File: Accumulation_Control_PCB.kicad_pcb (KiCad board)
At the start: 4 copper layers, 237.7 x 87.4 mm, 244 parts

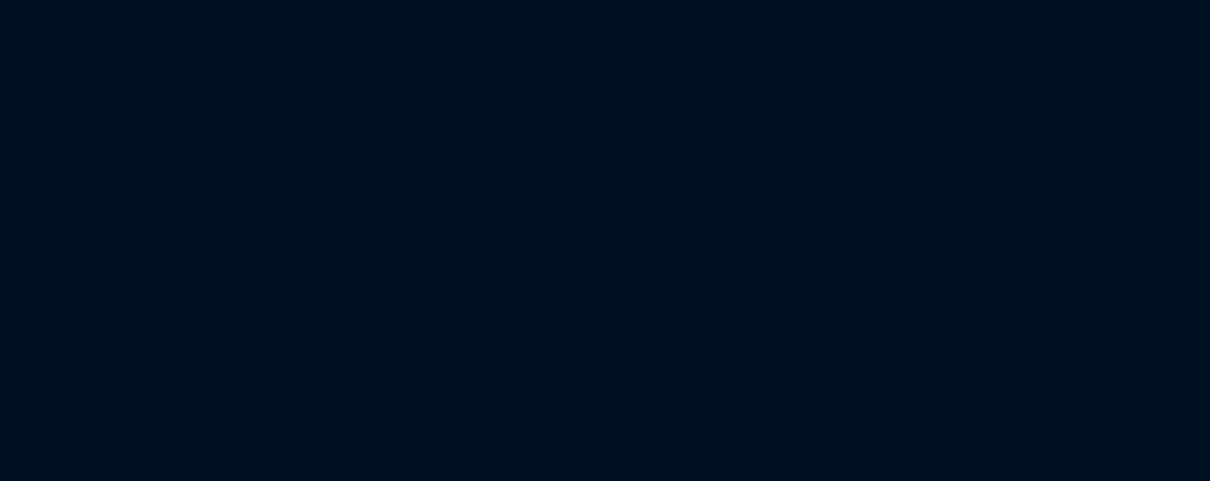
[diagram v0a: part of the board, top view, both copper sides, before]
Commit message: VER1.0: добавил один канал управления клапаном
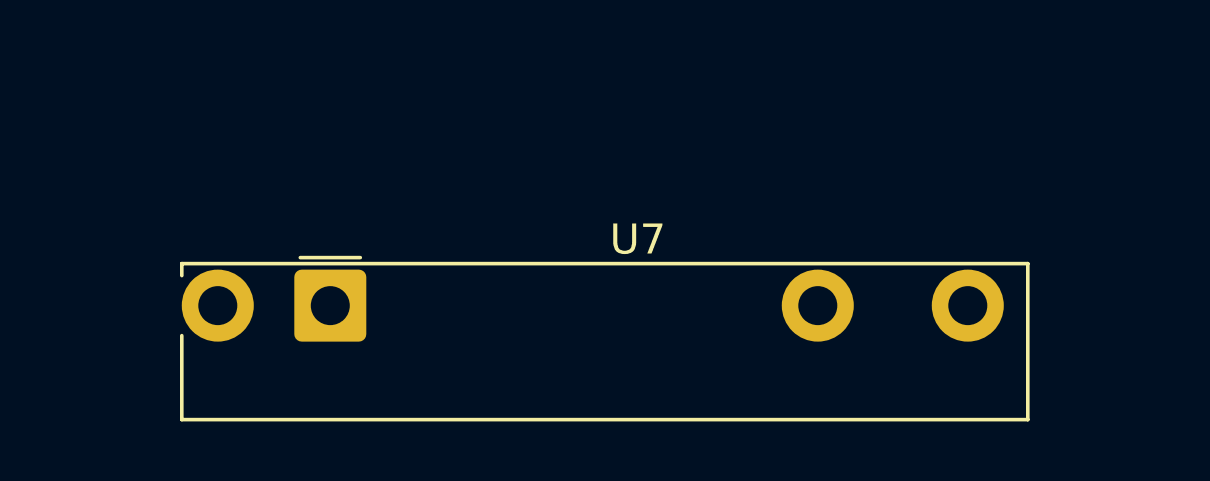
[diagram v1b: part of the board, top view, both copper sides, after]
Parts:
- added U7: 34.81-7048, OptoDevice:Finder_34.81, F.Cu at (313.8, 260.2)
- D44: value BZT52C10 -> ~

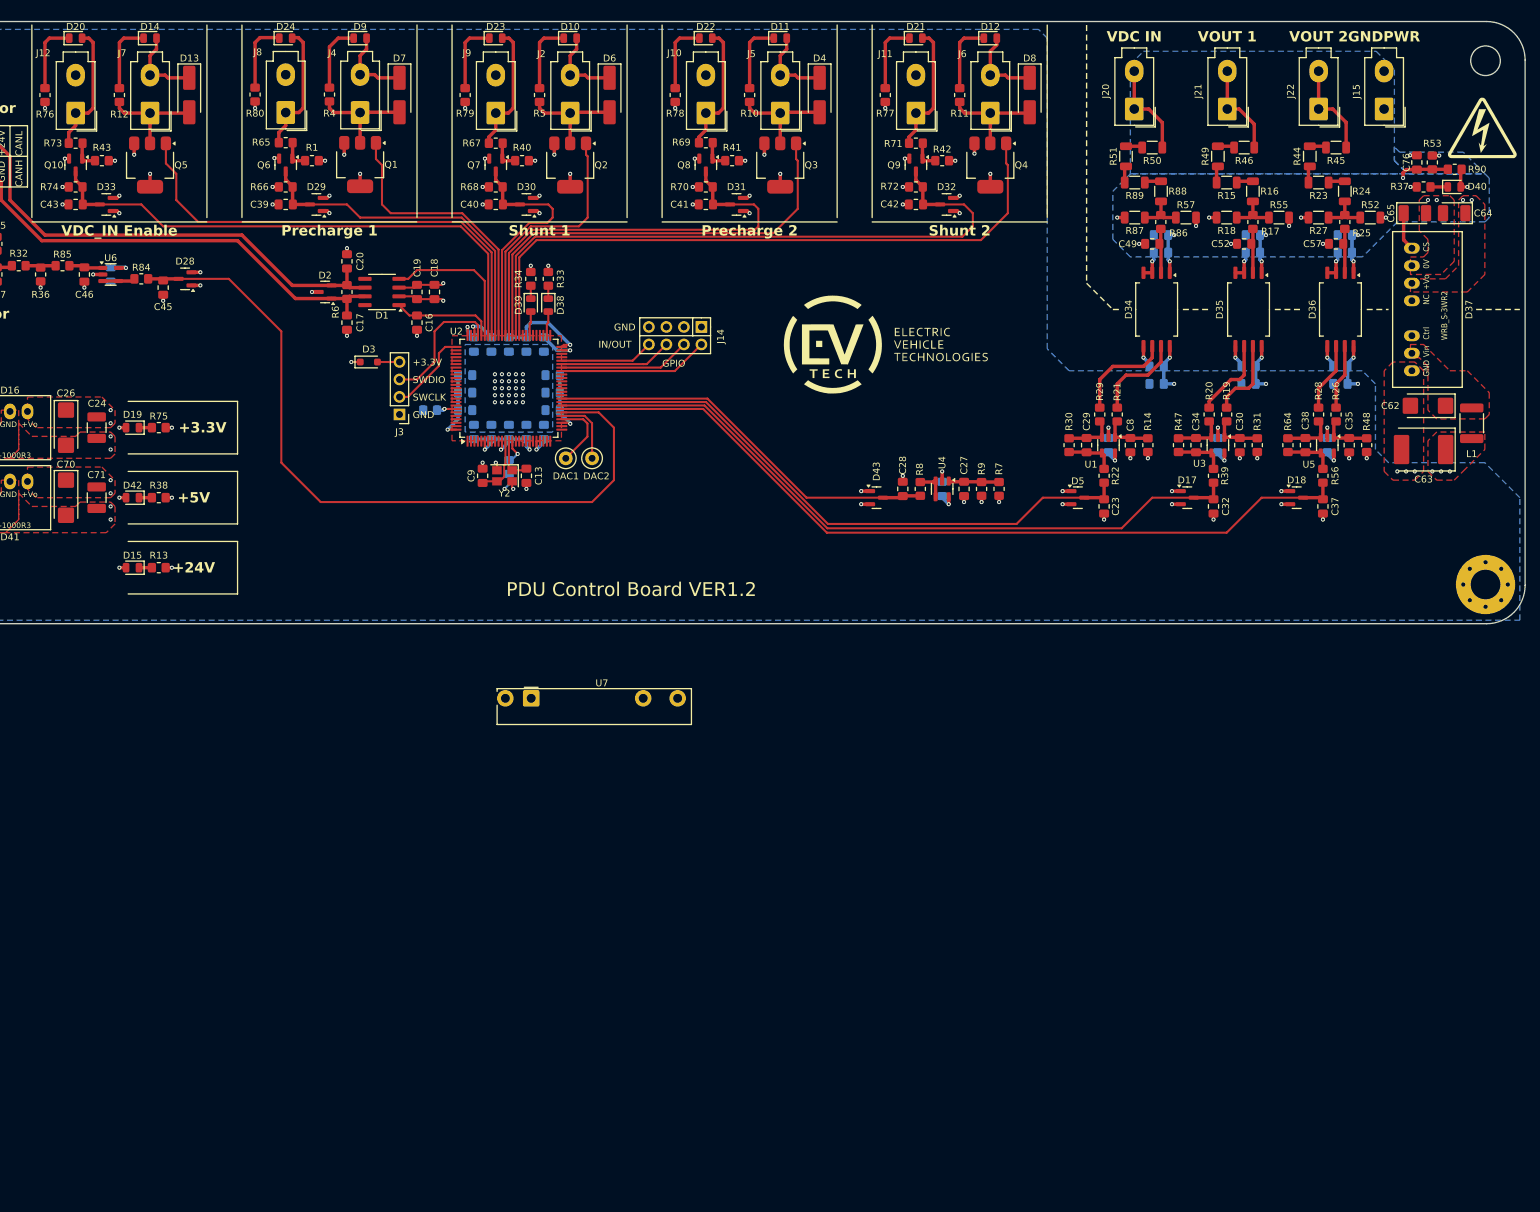
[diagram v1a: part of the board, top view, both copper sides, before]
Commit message: VER1.0: размножил на 8 каналов всего, отвязал 24Въ
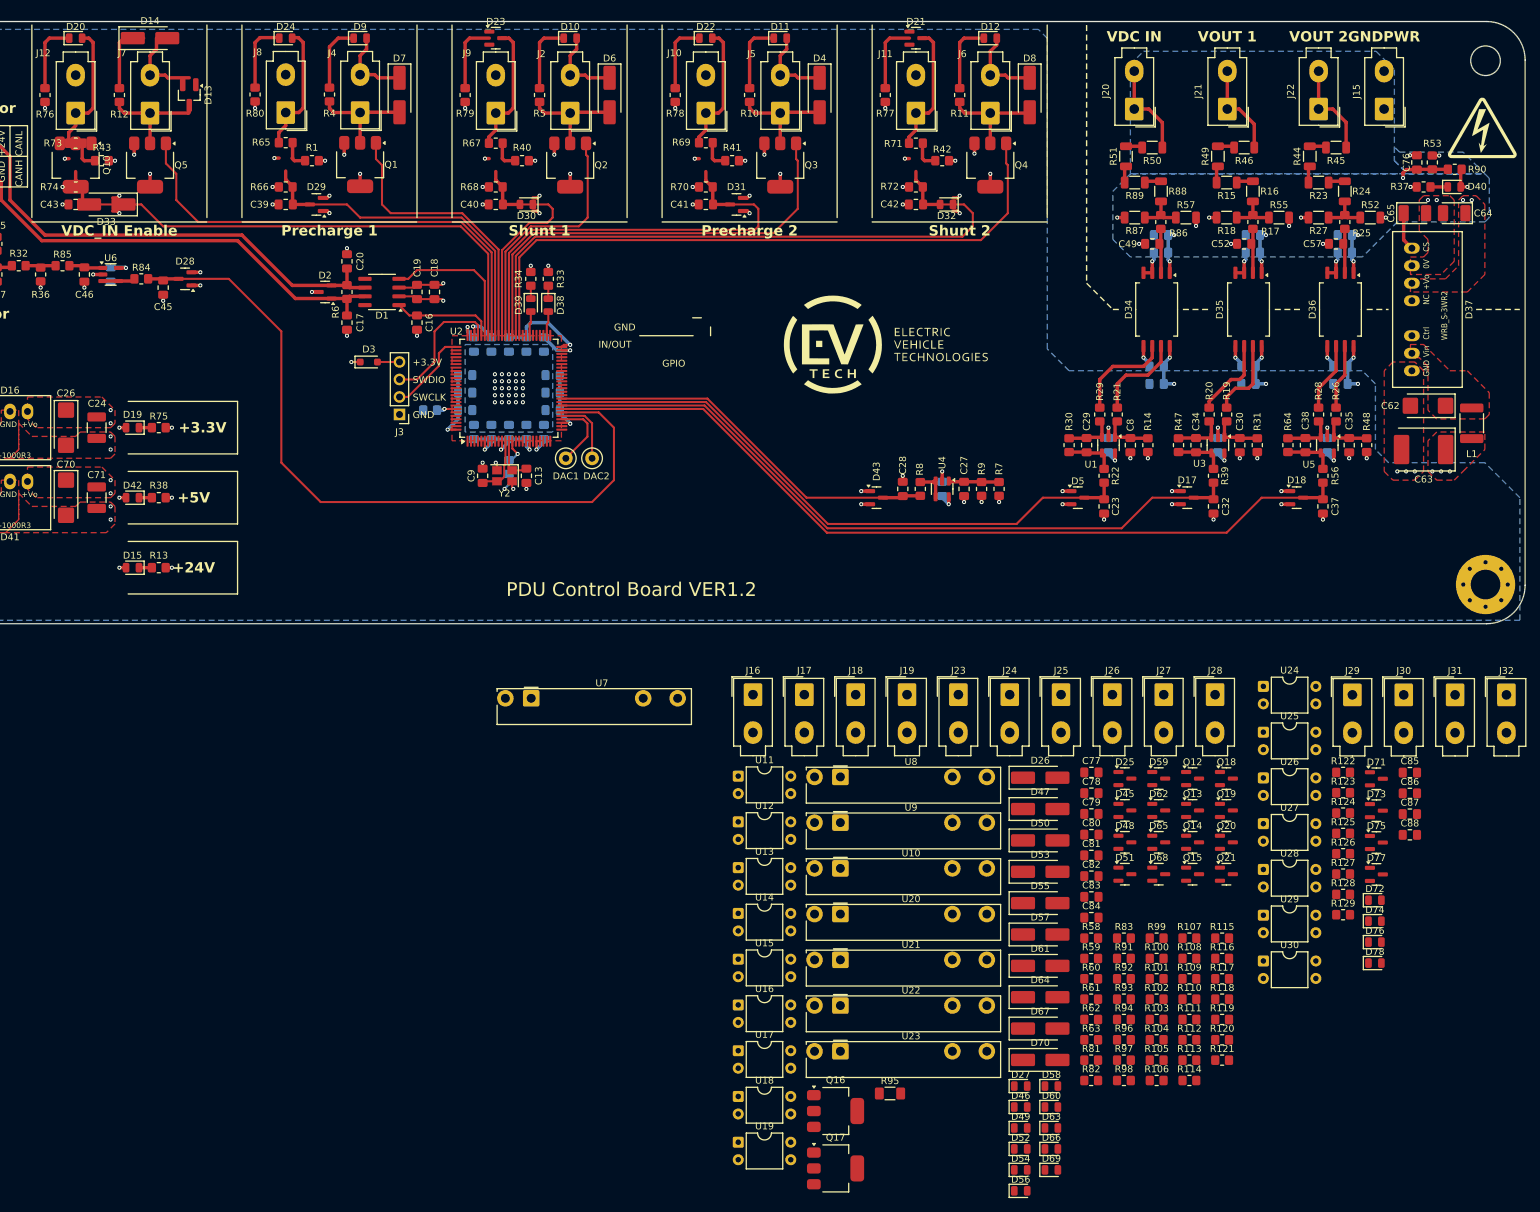
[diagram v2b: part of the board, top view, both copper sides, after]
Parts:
- removed J14: ~, Connector_PinHeader_2.54mm:PinHeader_2x04_P2.54mm_Vertical
- removed Q6, Q7, Q8, Q9: ~, Package_TO_SOT_SMD:SOT-23
- added C77: 100n, Capacitor_SMD:C_0805_2012Metric_Pad1.18x1.45mm_HandSolder, F.Cu at (395.0, 271.0)
- added C78: 100n, Capacitor_SMD:C_0805_2012Metric_Pad1.18x1.45mm_HandSolder, F.Cu at (395.0, 274.0)
- added C79: 100n, Capacitor_SMD:C_0805_2012Metric_Pad1.18x1.45mm_HandSolder, F.Cu at (395.0, 277.0)
- added C80: 100n, Capacitor_SMD:C_0805_2012Metric_Pad1.18x1.45mm_HandSolder, F.Cu at (395.0, 280.0)
- added C81: 1u, Capacitor_SMD:C_0805_2012Metric_Pad1.18x1.45mm_HandSolder, F.Cu at (395.0, 283.0)
- added C82: 100n, Capacitor_SMD:C_0805_2012Metric_Pad1.18x1.45mm_HandSolder, F.Cu at (395.0, 286.1)
- added C83: 100n, Capacitor_SMD:C_0805_2012Metric_Pad1.18x1.45mm_HandSolder, F.Cu at (395.0, 289.1)
- added C84: 100n, Capacitor_SMD:C_0805_2012Metric_Pad1.18x1.45mm_HandSolder, F.Cu at (395.0, 292.1)
- added C85: 1u, Capacitor_SMD:C_0805_2012Metric_Pad1.18x1.45mm_HandSolder, F.Cu at (441.2, 271.0)
- added C86: 1u, Capacitor_SMD:C_0805_2012Metric_Pad1.18x1.45mm_HandSolder, F.Cu at (441.2, 274.0)
- added C87: 1u, Capacitor_SMD:C_0805_2012Metric_Pad1.18x1.45mm_HandSolder, F.Cu at (441.2, 277.1)
- added C88: 1u, Capacitor_SMD:C_0805_2012Metric_Pad1.18x1.45mm_HandSolder, F.Cu at (441.2, 280.1)
- added D25: ~, Package_TO_SOT_SMD:SOT-23, F.Cu at (399.9, 271.9)
- added D26: ~, Diode_SMD:D_SMA_Handsoldering, F.Cu at (387.6, 271.8)
- added D27: ~, LED_SMD:LED_0805_2012Metric, F.Cu at (384.8, 316.5)
- added D45: ~, Package_TO_SOT_SMD:SOT-23, F.Cu at (399.9, 276.5)
- added D46: ~, LED_SMD:LED_0805_2012Metric, F.Cu at (384.8, 319.6)
- added D47: ~, Diode_SMD:D_SMA_Handsoldering, F.Cu at (387.6, 276.3)
- added D48: ~, Package_TO_SOT_SMD:SOT-23, F.Cu at (399.9, 281.1)
- added D49: ~, LED_SMD:LED_0805_2012Metric, F.Cu at (384.8, 322.6)
- added D50: ~, Diode_SMD:D_SMA_Handsoldering, F.Cu at (387.6, 280.9)
- added D51: ~, Package_TO_SOT_SMD:SOT-23, F.Cu at (399.9, 285.8)
- added D52: ~, LED_SMD:LED_0805_2012Metric, F.Cu at (384.8, 325.6)
- added D53: ~, Diode_SMD:D_SMA_Handsoldering, F.Cu at (387.6, 285.4)
- added D54: ~, LED_SMD:LED_0805_2012Metric, F.Cu at (384.8, 328.7)
- added D55: ~, Diode_SMD:D_SMA_Handsoldering, F.Cu at (387.6, 290.0)
- added D56: ~, LED_SMD:LED_0805_2012Metric, F.Cu at (384.8, 331.7)
- added D57: ~, Diode_SMD:D_SMA_Handsoldering, F.Cu at (387.6, 294.5)
- added D58: ~, LED_SMD:LED_0805_2012Metric, F.Cu at (389.2, 316.5)
- added D59: ~, Package_TO_SOT_SMD:SOT-23, F.Cu at (404.8, 271.9)
- added D60: ~, LED_SMD:LED_0805_2012Metric, F.Cu at (389.2, 319.6)
- added D61: ~, Diode_SMD:D_SMA_Handsoldering, F.Cu at (387.6, 299.1)
- added D62: ~, Package_TO_SOT_SMD:SOT-23, F.Cu at (404.8, 276.5)
- added D63: ~, LED_SMD:LED_0805_2012Metric, F.Cu at (389.2, 322.6)
- added D64: ~, Diode_SMD:D_SMA_Handsoldering, F.Cu at (387.6, 303.6)
- added D65: ~, Package_TO_SOT_SMD:SOT-23, F.Cu at (404.8, 281.1)
- added D66: ~, LED_SMD:LED_0805_2012Metric, F.Cu at (389.2, 325.6)
- added D67: ~, Diode_SMD:D_SMA_Handsoldering, F.Cu at (387.6, 308.2)
- added D68: ~, Package_TO_SOT_SMD:SOT-23, F.Cu at (404.8, 285.8)
- added D69: ~, LED_SMD:LED_0805_2012Metric, F.Cu at (389.2, 328.7)
- added D70: ~, Diode_SMD:D_SMA_Handsoldering, F.Cu at (387.6, 312.7)
- added D71: ~, Package_TO_SOT_SMD:SOT-23, F.Cu at (436.4, 271.9)
- added D72: ~, LED_SMD:LED_0805_2012Metric, F.Cu at (436.2, 289.5)
- added D73: ~, Package_TO_SOT_SMD:SOT-23, F.Cu at (436.4, 276.6)
- added D74: ~, LED_SMD:LED_0805_2012Metric, F.Cu at (436.2, 292.6)
- added D75: ~, Package_TO_SOT_SMD:SOT-23, F.Cu at (436.4, 281.2)
- added D76: ~, LED_SMD:LED_0805_2012Metric, F.Cu at (436.2, 295.6)
- added D77: ~, Package_TO_SOT_SMD:SOT-23, F.Cu at (436.4, 285.8)
- added D78: ~, LED_SMD:LED_0805_2012Metric, F.Cu at (436.2, 298.7)
- added J16: ~, Connector_My:Mini-Fit_01x02_Vertical, F.Cu at (345.9, 259.7)
- added J17: ~, Connector_My:Mini-Fit_01x02_Vertical, F.Cu at (353.4, 259.7)
- added J18: ~, Connector_My:Mini-Fit_01x02_Vertical, F.Cu at (360.8, 259.7)
- added J19: ~, Connector_My:Mini-Fit_01x02_Vertical, F.Cu at (368.3, 259.7)
- added J23: ~, Connector_My:Mini-Fit_01x02_Vertical, F.Cu at (375.7, 259.7)
- added J24: ~, Connector_My:Mini-Fit_01x02_Vertical, F.Cu at (383.2, 259.7)
- added J25: ~, Connector_My:Mini-Fit_01x02_Vertical, F.Cu at (390.6, 259.7)
- added J26: ~, Connector_My:Mini-Fit_01x02_Vertical, F.Cu at (398.1, 259.7)
- added J27: ~, Connector_My:Mini-Fit_01x02_Vertical, F.Cu at (405.5, 259.7)
- added J28: ~, Connector_My:Mini-Fit_01x02_Vertical, F.Cu at (413.0, 259.7)
- added J29: ~, Connector_My:Mini-Fit_01x02_Vertical, F.Cu at (432.9, 259.8)
- added J30: ~, Connector_My:Mini-Fit_01x02_Vertical, F.Cu at (440.4, 259.8)
- added J31: ~, Connector_My:Mini-Fit_01x02_Vertical, F.Cu at (447.8, 259.8)
- added J32: ~, Connector_My:Mini-Fit_01x02_Vertical, F.Cu at (455.2, 259.8)
- added Q12: ~, Package_TO_SOT_SMD:SOT-23, F.Cu at (409.7, 271.9)
- added Q13: ~, Package_TO_SOT_SMD:SOT-23, F.Cu at (409.7, 276.5)
- added Q14: ~, Package_TO_SOT_SMD:SOT-23, F.Cu at (409.7, 281.1)
- added Q15: ~, Package_TO_SOT_SMD:SOT-23, F.Cu at (409.7, 285.8)
- added Q16: ~, Package_TO_SOT_SMD:SOT-223, F.Cu at (357.9, 320.1)
- added Q17: ~, Package_TO_SOT_SMD:SOT-223, F.Cu at (357.9, 328.5)
- added Q18: ~, Package_TO_SOT_SMD:SOT-23, F.Cu at (414.6, 271.9)
- added Q19: ~, Package_TO_SOT_SMD:SOT-23, F.Cu at (414.6, 276.5)
- added Q20: ~, Package_TO_SOT_SMD:SOT-23, F.Cu at (414.6, 281.1)
- added Q21: ~, Package_TO_SOT_SMD:SOT-23, F.Cu at (414.6, 285.8)
- added R100: 330, Resistor_SMD:R_0805_2012Metric_Pad1.20x1.40mm_HandSolder, F.Cu at (404.5, 298.0)
- added R101: 10k, Resistor_SMD:R_0805_2012Metric_Pad1.20x1.40mm_HandSolder, F.Cu at (404.5, 300.9)
- added R102: 8.2k, Resistor_SMD:R_0805_2012Metric_Pad1.20x1.40mm_HandSolder, F.Cu at (404.5, 303.9)
- added R103: 10k, Resistor_SMD:R_0805_2012Metric_Pad1.20x1.40mm_HandSolder, F.Cu at (404.5, 306.9)
- added R104: 330, Resistor_SMD:R_0805_2012Metric_Pad1.20x1.40mm_HandSolder, F.Cu at (404.5, 309.8)
- added R105: 8.2k, Resistor_SMD:R_0805_2012Metric_Pad1.20x1.40mm_HandSolder, F.Cu at (404.5, 312.8)
- added R106: 10k, Resistor_SMD:R_0805_2012Metric_Pad1.20x1.40mm_HandSolder, F.Cu at (404.5, 315.7)
- added R107: 330, Resistor_SMD:R_0805_2012Metric_Pad1.20x1.40mm_HandSolder, F.Cu at (409.2, 295.1)
- added R108: 8.2k, Resistor_SMD:R_0805_2012Metric_Pad1.20x1.40mm_HandSolder, F.Cu at (409.2, 298.0)
- added R109: 10k, Resistor_SMD:R_0805_2012Metric_Pad1.20x1.40mm_HandSolder, F.Cu at (409.2, 300.9)
- added R110: 1k, Resistor_SMD:R_0805_2012Metric_Pad1.20x1.40mm_HandSolder, F.Cu at (409.2, 303.9)
- added R111: 8.2k, Resistor_SMD:R_0805_2012Metric_Pad1.20x1.40mm_HandSolder, F.Cu at (409.2, 306.9)
- added R112: 10k, Resistor_SMD:R_0805_2012Metric_Pad1.20x1.40mm_HandSolder, F.Cu at (409.2, 309.8)
- added R113: 1k, Resistor_SMD:R_0805_2012Metric_Pad1.20x1.40mm_HandSolder, F.Cu at (409.2, 312.8)
- added R114: 8.2k, Resistor_SMD:R_0805_2012Metric_Pad1.20x1.40mm_HandSolder, F.Cu at (409.2, 315.7)
- added R115: 10k, Resistor_SMD:R_0805_2012Metric_Pad1.20x1.40mm_HandSolder, F.Cu at (414.0, 295.1)
- added R116: 1k, Resistor_SMD:R_0805_2012Metric_Pad1.20x1.40mm_HandSolder, F.Cu at (414.0, 298.0)
- added R117: 8.2k, Resistor_SMD:R_0805_2012Metric_Pad1.20x1.40mm_HandSolder, F.Cu at (414.0, 300.9)
- added R118: 10k, Resistor_SMD:R_0805_2012Metric_Pad1.20x1.40mm_HandSolder, F.Cu at (414.0, 303.9)
- added R119: 1k, Resistor_SMD:R_0805_2012Metric_Pad1.20x1.40mm_HandSolder, F.Cu at (414.0, 306.9)
- added R120: 8.2k, Resistor_SMD:R_0805_2012Metric_Pad1.20x1.40mm_HandSolder, F.Cu at (414.0, 309.8)
- added R121: 10k, Resistor_SMD:R_0805_2012Metric_Pad1.20x1.40mm_HandSolder, F.Cu at (414.0, 312.8)
- added R122: 3.3k, Resistor_SMD:R_0805_2012Metric_Pad1.20x1.40mm_HandSolder, F.Cu at (431.6, 271.0)
- added R123: 10k, Resistor_SMD:R_0805_2012Metric_Pad1.20x1.40mm_HandSolder, F.Cu at (431.6, 273.9)
- added R124: 3.3k, Resistor_SMD:R_0805_2012Metric_Pad1.20x1.40mm_HandSolder, F.Cu at (431.6, 276.9)
- added R125: 8.2k, Resistor_SMD:R_0805_2012Metric_Pad1.20x1.40mm_HandSolder, F.Cu at (431.6, 279.9)
- added R126: 10k, Resistor_SMD:R_0805_2012Metric_Pad1.20x1.40mm_HandSolder, F.Cu at (431.6, 282.8)
- added R127: 3.3k, Resistor_SMD:R_0805_2012Metric_Pad1.20x1.40mm_HandSolder, F.Cu at (431.6, 285.8)
- added R128: 8.2k, Resistor_SMD:R_0805_2012Metric_Pad1.20x1.40mm_HandSolder, F.Cu at (431.6, 288.7)
- added R129: 10k, Resistor_SMD:R_0805_2012Metric_Pad1.20x1.40mm_HandSolder, F.Cu at (431.6, 291.6)
- added R58: 8.2k, Resistor_SMD:R_0805_2012Metric_Pad1.20x1.40mm_HandSolder, F.Cu at (395.0, 295.1)
- added R59: 1k, Resistor_SMD:R_0805_2012Metric_Pad1.20x1.40mm_HandSolder, F.Cu at (395.0, 298.0)
- added R60: 10k, Resistor_SMD:R_0805_2012Metric_Pad1.20x1.40mm_HandSolder, F.Cu at (395.0, 300.9)
- added R61: 1k, Resistor_SMD:R_0805_2012Metric_Pad1.20x1.40mm_HandSolder, F.Cu at (395.0, 303.9)
- added R62: 8.2k, Resistor_SMD:R_0805_2012Metric_Pad1.20x1.40mm_HandSolder, F.Cu at (395.0, 306.9)
- added R63: 10k, Resistor_SMD:R_0805_2012Metric_Pad1.20x1.40mm_HandSolder, F.Cu at (395.0, 309.8)
- added R81: 1k, Resistor_SMD:R_0805_2012Metric_Pad1.20x1.40mm_HandSolder, F.Cu at (395.0, 312.8)
- added R82: 8.2k, Resistor_SMD:R_0805_2012Metric_Pad1.20x1.40mm_HandSolder, F.Cu at (395.0, 315.7)
- added R83: 10k, Resistor_SMD:R_0805_2012Metric_Pad1.20x1.40mm_HandSolder, F.Cu at (399.8, 295.1)
- added R91: 1k, Resistor_SMD:R_0805_2012Metric_Pad1.20x1.40mm_HandSolder, F.Cu at (399.8, 298.0)
- added R92: 8.2k, Resistor_SMD:R_0805_2012Metric_Pad1.20x1.40mm_HandSolder, F.Cu at (399.8, 300.9)
- added R93: 10k, Resistor_SMD:R_0805_2012Metric_Pad1.20x1.40mm_HandSolder, F.Cu at (399.8, 303.9)
- added R94: 330, Resistor_SMD:R_0805_2012Metric_Pad1.20x1.40mm_HandSolder, F.Cu at (399.8, 306.9)
- added R95: 2.4k, Resistor_SMD:R_1206_3216Metric_Pad1.30x1.75mm_HandSolder, F.Cu at (365.8, 317.6)
- added R96: 330, Resistor_SMD:R_0805_2012Metric_Pad1.20x1.40mm_HandSolder, F.Cu at (399.8, 309.8)
- added R97: 10k, Resistor_SMD:R_0805_2012Metric_Pad1.20x1.40mm_HandSolder, F.Cu at (399.8, 312.8)
- added R98: 330, Resistor_SMD:R_0805_2012Metric_Pad1.20x1.40mm_HandSolder, F.Cu at (399.8, 315.7)
- added R99: 10k, Resistor_SMD:R_0805_2012Metric_Pad1.20x1.40mm_HandSolder, F.Cu at (404.5, 295.1)
- added U10: RSCD06D3, OptoDevice:Finder_34.81, F.Cu at (358.6, 284.9)
- added U11: PC817, Package_DIP:DIP-4_W7.62mm, F.Cu at (343.8, 271.5)
- added U12: PC817, Package_DIP:DIP-4_W7.62mm, F.Cu at (343.8, 278.2)
- added U13: PC817, Package_DIP:DIP-4_W7.62mm, F.Cu at (343.8, 284.8)
- added U14: PC817, Package_DIP:DIP-4_W7.62mm, F.Cu at (343.8, 291.5)
- added U15: PC817, Package_DIP:DIP-4_W7.62mm, F.Cu at (343.8, 298.1)
- added U16: PC817, Package_DIP:DIP-4_W7.62mm, F.Cu at (343.8, 304.7)
- added U17: PC817, Package_DIP:DIP-4_W7.62mm, F.Cu at (343.8, 311.4)
- added U18: PC817, Package_DIP:DIP-4_W7.62mm, F.Cu at (343.8, 318.0)
- added U19: PC817, Package_DIP:DIP-4_W7.62mm, F.Cu at (343.8, 324.7)
- added U20: RSCD06D3, OptoDevice:Finder_34.81, F.Cu at (358.6, 291.6)
- added U21: RSCD06D3, OptoDevice:Finder_34.81, F.Cu at (358.6, 298.2)
- added U22: RSCD06D3, OptoDevice:Finder_34.81, F.Cu at (358.6, 304.8)
- added U23: RSCD06D3, OptoDevice:Finder_34.81, F.Cu at (358.6, 311.5)
- added U24: PC817, Package_DIP:DIP-4_W7.62mm, F.Cu at (420.0, 258.5)
- added U25: PC817, Package_DIP:DIP-4_W7.62mm, F.Cu at (420.0, 265.2)
- added U26: PC817, Package_DIP:DIP-4_W7.62mm, F.Cu at (420.0, 271.8)
- added U27: PC817, Package_DIP:DIP-4_W7.62mm, F.Cu at (420.0, 278.4)
- added U28: PC817, Package_DIP:DIP-4_W7.62mm, F.Cu at (420.0, 285.1)
- added U29: PC817, Package_DIP:DIP-4_W7.62mm, F.Cu at (420.0, 291.7)
- added U30: PC817, Package_DIP:DIP-4_W7.62mm, F.Cu at (420.0, 298.4)
- added U8: RSCD06D3, OptoDevice:Finder_34.81, F.Cu at (358.6, 271.7)
- added U9: RSCD06D3, OptoDevice:Finder_34.81, F.Cu at (358.6, 278.3)
- C43: value 1u -> 100n
- D13: value ~ -> BZX84C5V1; footprint Diode_SMD:D_SMA_Handsoldering -> Package_TO_SOT_SMD:SOT-23_Handsoldering
- D14: footprint LED_SMD:LED_0805_2012Metric -> Diode_SMD:D_SMA_Handsoldering
- D21, D23: footprint LED_SMD:LED_0805_2012Metric -> Package_TO_SOT_SMD:SOT-23
- D30, D32: footprint Package_TO_SOT_SMD:SOT-23 -> LED_SMD:LED_0805_2012Metric
- D33: footprint Package_TO_SOT_SMD:SOT-23 -> Diode_SMD:D_SMA_Handsoldering
- Q10: footprint Package_TO_SOT_SMD:SOT-23 -> Package_TO_SOT_SMD:SOT-223
- R12, R77: value 8.2k -> 10k
- R40, R65, R71: value 10k -> 3.3k
- R41, R69, R73: value 10k -> 8.2k
- R43: value 10k -> 330
- R66, R72: value 100 -> 8.2k
- R68: value 100 -> 3.3k
- R70, R74: value 100 -> 10k
- R76: value 8.2k -> 330
- R78: value 8.2k -> 3.3k
- U7: value 34.81-7048 -> RSCD06D3
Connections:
- C39 pad 1: ~{Precharge_1_ON} -> Relay_1_ON
- C40 pad 1: ~{Shunt_1_ON} -> Relay_2_ON
- C41 pad 1: ~{Precharge_2_ON} -> Relay_3_ON
- C42 pad 1: ~{Shunt_2_ON} -> Relay_4_ON
- C43 pad 1: ~{VIN_Enable_ON} -> Coil_5_CTRL
- D13 pad 1: +24V -> +5.1V
- D13 pad 2: Net-(D13-A) -> GNDPWR
- D14 pad 1: Net-(D14-K) -> +24V
- D14 pad 2: +24V -> Net-(D14-A)
- D20 pad 2: Net-(D20-A) -> +24V
- D21 pad 1: Net-(D21-K) -> GND
- D21 pad 2: Net-(D21-A) -> +3.3V
- D23 pad 1: Net-(D23-K) -> GND
- D23 pad 2: Net-(D23-A) -> +3.3V
- D29 pad 3: ~{Precharge_1_ON} -> Relay_1_ON
- D30 pad 1: GND -> Net-(D30-K)
- D30 pad 2: +3.3V -> Net-(D30-A)
- D31 pad 3: ~{Precharge_2_ON} -> Relay_4_ON
- D32 pad 1: GND -> Net-(D32-K)
- D32 pad 2: +3.3V -> Net-(D32-A)
- D33 pad 1: GND -> Net-(D33-K)
- D33 pad 2: +3.3V -> Net-(D33-A)
- D6 pad 1: +24V -> Net-(D6-K)
- J10 pad 1: Net-(D22-A) -> Net-(D30-A)
- J11 pad 1: Net-(D21-A) -> Net-(D32-A)
- J12 pad 1: Net-(D20-A) -> Net-(D33-A)
- J12 pad 2: +24V -> Net-(D33-K)
- J2 pad 2: +24V -> Net-(D6-K)
- J7 pad 1: Net-(D13-A) -> Net-(D14-A)
- J9 pad 1: Net-(D23-A) -> Net-(D22-A)
- Q1 pad 1: Precharge_1 -> Net-(Q1-G)
- Q1 pad 3: GND -> GNDPWR
- Q1 pad 4: GND -> GNDPWR
- Q10 pad 2: GND -> Net-(D33-A)
- Q10 pad 3: ~{VIN_Enable_ON} -> GNDPWR
- Q2 pad 1: Shunt_1 -> Net-(Q2-G)
- Q2 pad 3: GND -> GNDPWR
- Q2 pad 4: GND -> GNDPWR
- Q3 pad 1: Precharge_2 -> Net-(Q3-G)
- Q3 pad 3: GND -> GNDPWR
- Q3 pad 4: GND -> GNDPWR
- Q4 pad 1: Shunt_2 -> Net-(Q4-G)
- Q4 pad 3: GND -> GNDPWR
- Q4 pad 4: GND -> GNDPWR
- Q5 pad 1: VIN_Enable -> Net-(Q5-G)
- Q5 pad 2: Net-(D13-A) -> Net-(D14-A)
- Q5 pad 3: GND -> GNDPWR
- Q5 pad 4: GND -> GNDPWR
- R1 pad 1: GND -> Relay_1_ON
- R1 pad 2: Net-(Q6-G) -> GND
- R12 pad 1: Net-(D14-K) -> GNDPWR
- R12 pad 2: Net-(D13-A) -> Net-(Q1-G)
- R40 pad 1: GND -> Net-(R40-Pad1)
- R40 pad 2: Net-(Q7-G) -> Net-(D22-A)
- R41 pad 1: GND -> Net-(D22-K)
- R41 pad 2: Net-(Q8-G) -> GNDPWR
- R42 pad 1: Net-(Q9-G) -> Relay_2_ON
- R43 pad 1: GND -> Relay_5
- R43 pad 2: Net-(Q10-G) -> Net-(R43-Pad2)
- R65 pad 1: Net-(D24-A) -> Net-(R65-Pad1)
- R65 pad 2: Net-(Q6-G) -> Net-(D30-A)
- R66 pad 1: ~{Precharge_1_ON} -> Net-(D30-K)
- R66 pad 2: +3.3V -> GNDPWR
- R67 pad 1: Net-(D23-A) -> Relay_3_ON
- R67 pad 2: Net-(Q7-G) -> GND
- R68 pad 1: ~{Shunt_1_ON} -> Net-(R68-Pad1)
- R68 pad 2: +3.3V -> Net-(D32-A)
- R69 pad 1: Net-(D22-A) -> Net-(D32-K)
- R69 pad 2: Net-(Q8-G) -> GNDPWR
- R70 pad 1: ~{Precharge_2_ON} -> Relay_4_ON
- R70 pad 2: +3.3V -> GND
- R71 pad 1: Net-(D21-A) -> Net-(R71-Pad1)
- R71 pad 2: Net-(Q9-G) -> Net-(D72-A)
- R72 pad 1: ~{Shunt_2_ON} -> Net-(D72-K)
- R72 pad 2: +3.3V -> GNDPWR
- R73 pad 1: Net-(D20-A) -> Net-(D20-K)
- R73 pad 2: Net-(Q10-G) -> Net-(D14-A)
- R74 pad 1: ~{VIN_Enable_ON} -> GNDPWR
- R74 pad 2: +3.3V -> Net-(Q5-G)
- R76 pad 1: Net-(D20-K) -> Relay_6
- R76 pad 2: GND -> Net-(R76-Pad2)
- R77 pad 1: Net-(D21-K) -> Relay_5_ON
- R78 pad 1: Net-(D22-K) -> Net-(R78-Pad1)
- R78 pad 2: GND -> Net-(D74-A)
- R79 pad 1: Net-(D23-K) -> Net-(D74-K)
- R79 pad 2: GND -> GNDPWR
- R80 pad 2: GND -> GNDPWR
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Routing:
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
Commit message: VER1.0: изолировал питание 5В и CAN
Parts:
- removed C48: 2.2u, Capacitor_SMD:C_0805_2012Metric_Pad1.18x1.45mm_HandSolder
- removed C49: 56p, Capacitor_SMD:C_0805_2012Metric_Pad1.18x1.45mm_HandSolder
- removed the G*** at (365.1, 208.9)
- removed J32: ~, Connector_My:Mini-Fit_01x02_Vertical
- removed Q18, Q19, Q20, Q21: ~, Package_TO_SOT_SMD:SOT-23
- removed Y2: ~, Crystal:Crystal_SMD_SeikoEpson_FA238-4Pin_3.2x2.5mm
- added C89: 100n, Capacitor_SMD:C_0805_2012Metric_Pad1.18x1.45mm_HandSolder, F.Cu at (242.9, 271.9)
- added C90: 1u, Capacitor_SMD:C_0805_2012Metric_Pad1.18x1.45mm_HandSolder, F.Cu at (242.9, 274.9)
- added C91: 100n, Capacitor_SMD:C_0805_2012Metric_Pad1.18x1.45mm_HandSolder, F.Cu at (242.9, 277.9)
- added D79: ~, LED_SMD:LED_0805_2012Metric, F.Cu at (152.1, 275.8)
- added J14: ~, Connector_My:Mini-Fit_01x02_Vertical, F.Cu at (244.2, 260.6)
- added L2: ~, Inductor_SMD:L_CommonModeChoke_Murata_DLW5BTMxxxSQ2x_5x5mm, B.Cu at (227.8, 205.0)
- added L3: ~, Inductor_SMD:L_CommonModeChoke_TDK_ACM2520-2P, F.Cu at (246.8, 203.8)
- added Q6: ~, Package_TO_SOT_SMD:SOT-223, F.Cu at (235.5, 261.6)
- added Q7: ~, Package_TO_SOT_SMD:SOT-23, F.Cu at (250.4, 259.8)
- added Q8: ~, Package_TO_SOT_SMD:SOT-223, F.Cu at (235.5, 269.9)
- added Q9: ~, Package_TO_SOT_SMD:SOT-23, F.Cu at (250.4, 264.4)
- added R130: 8.2k, Resistor_SMD:R_0805_2012Metric_Pad1.20x1.40mm_HandSolder, F.Cu at (152.2, 272.8)
- added R131: 59, Resistor_SMD:R_0805_2012Metric_Pad1.20x1.40mm_HandSolder, F.Cu at (251.0, 205.5)
- added Y1: ~, Crystal:Crystal_SMD_SeikoEpson_FA238-4Pin_3.2x2.5mm, F.Cu at (247.9, 272.7)
- C1, C12, C21, C36: value 100n -> 56p
- C10: value 100n -> 0.27u
- C13: value 30p -> 47n
- C14: value 2.2u -> 2.2n
- C15: value 2.2u -> 56p
- C16, C17, C28, C29, C35, C8: value 56p -> 100n
- C18, C19, C2, C81, C85, C87: value 1u -> 100n
- C20: value 56p -> 0.27u
- C22: value 100n -> 2.2u
- C23: value 0.27u -> 0.1u
- C24: value 22u -> 2.2u; footprint Capacitor_SMD:C_1210_3225Metric_Pad1.33x2.70mm_HandSolder -> Capacitor_SMD:C_0805_2012Metric_Pad1.18x1.45mm_HandSolder
- C25: value 10u -> 0.1u; footprint Capacitor_SMD:C_1210_3225Metric_Pad1.33x2.70mm_HandSolder -> Capacitor_SMD:C_0805_2012Metric_Pad1.18x1.45mm_HandSolder
- C26: value 330u -> 30p; footprint Capacitor_Tantalum_SMD:CP_EIA-6032-28_Kemet-C_Pad2.25x2.35mm_HandSolder -> Capacitor_SMD:C_0805_2012Metric_Pad1.18x1.45mm_HandSolder
- C30: value 56p -> 30p
- C31: value 100n -> 4.7u
- C32: value 0.27u -> 100n
- C33: value 22u -> 100n; footprint Capacitor_Tantalum_SMD:CP_EIA-7343-43_Kemet-X_Pad2.25x2.55mm_HandSolder -> Capacitor_SMD:C_0805_2012Metric_Pad1.18x1.45mm_HandSolder
- C39, C41: value 1u -> 2.2u
- C4, C6, C75, C77, C80, C82, C84: value 100n -> 1u
- C40, C42: value 1u -> 0.1u
- C43: value 100n -> 22u
- C44: value 100n -> 10u; footprint Capacitor_SMD:C_0805_2012Metric_Pad1.18x1.45mm_HandSolder -> Capacitor_SMD:C_1210_3225Metric_Pad1.33x2.70mm_HandSolder
- C45: value 0.27u -> 330u
- C46: value 56p -> 22u; footprint Capacitor_SMD:C_0805_2012Metric_Pad1.18x1.45mm_HandSolder -> Capacitor_SMD:C_1210_3225Metric_Pad1.33x2.70mm_HandSolder
- C47: footprint Capacitor_SMD:C_0805_2012Metric_Pad1.18x1.45mm_HandSolder -> Capacitor_SMD:C_1206_3216Metric_Pad1.33x1.80mm_HandSolder
- C50: value 2.2u -> 10u; footprint Capacitor_SMD:C_0805_2012Metric_Pad1.18x1.45mm_HandSolder -> Capacitor_SMD:C_1206_3216Metric_Pad1.33x1.80mm_HandSolder
- C51: value 0.1u -> 10n
- C52: value 56p -> 2.2u
- C54, C56: value 0.1u -> 56p
- C55: value 2.2u -> 100n
- C57: value 56p -> 10u
- C58: value 2.2u -> 10u
- C59: value 0.1u -> 1u
- C60: value 2.2u -> 0.27u
- C61: value 0.1u -> 100u
- C62: value 1u -> 56p; footprint Capacitor_Tantalum_SMD:CP_EIA-6032-28_Kemet-C_Pad2.25x2.35mm_HandSolder -> Capacitor_SMD:C_0805_2012Metric_Pad1.18x1.45mm_HandSolder
- C63: value 10u -> 2.2u; footprint Capacitor_Tantalum_SMD:CP_EIA-7360-38_Kemet-E_Pad2.25x4.25mm_HandSolder -> Capacitor_SMD:C_0805_2012Metric_Pad1.18x1.45mm_HandSolder
- C64: value 100u -> 0.1u; footprint Capacitor_Tantalum_SMD:CP_EIA-3528-21_Kemet-B_Pad1.50x2.35mm_HandSolder -> Capacitor_SMD:C_0805_2012Metric_Pad1.18x1.45mm_HandSolder
- C65: value 10u -> 2.2u; footprint Capacitor_Tantalum_SMD:CP_EIA-3528-21_Kemet-B_Pad1.50x2.35mm_HandSolder -> Capacitor_SMD:C_0805_2012Metric_Pad1.18x1.45mm_HandSolder
- C66: value 22u -> 0.1u; footprint Capacitor_Tantalum_SMD:CP_EIA-7343-43_Kemet-X_Pad2.25x2.55mm_HandSolder -> Capacitor_SMD:C_0805_2012Metric_Pad1.18x1.45mm_HandSolder
- C67: value 2.2n -> 1n; footprint Capacitor_SMD:C_0805_2012Metric_Pad1.18x1.45mm_HandSolder -> Capacitor_THT:C_Disc_D7.0mm_W2.5mm_P5.00mm
- C68: value 47n -> 10u; footprint Capacitor_SMD:C_0805_2012Metric_Pad1.18x1.45mm_HandSolder -> Capacitor_SMD:C_1206_3216Metric_Pad1.33x1.80mm_HandSolder
- C69: value 10u -> 330u; footprint Capacitor_SMD:C_1210_3225Metric_Pad1.33x2.70mm_HandSolder -> Capacitor_THT:CP_Radial_D10.0mm_P5.00mm
- C70: value 330u -> 10u; footprint Capacitor_Tantalum_SMD:CP_EIA-6032-28_Kemet-C_Pad2.25x2.35mm_HandSolder -> Capacitor_SMD:C_1206_3216Metric_Pad1.33x1.80mm_HandSolder; moved to B.Cu
- C71: value 22u -> 10u; footprint Capacitor_SMD:C_1210_3225Metric_Pad1.33x2.70mm_HandSolder -> Capacitor_SMD:C_1206_3216Metric_Pad1.33x1.80mm_HandSolder; moved to B.Cu
- C72: value 1u -> 330u; footprint Capacitor_SMD:C_0805_2012Metric_Pad1.18x1.45mm_HandSolder -> Capacitor_THT:CP_Radial_D10.0mm_P5.00mm; moved to F.Cu
- C73: value 4.7u -> 1u
- C74: value 100n -> 1n; footprint Capacitor_SMD:C_0805_2012Metric_Pad1.18x1.45mm_HandSolder -> Capacitor_THT:C_Disc_D7.0mm_W2.5mm_P5.00mm; moved to F.Cu
- C9: value 30p -> 56p
- D1: footprint Package_SO:SOIC-8_3.9x4.9mm_P1.27mm -> Package_TO_SOT_SMD:SOT-23
- D10: footprint LED_SMD:LED_0805_2012Metric -> MORNSUN:K78xx-1000R3
- D13: value BZX84C5V1 -> TD301MCANFD; footprint Package_TO_SOT_SMD:SOT-23_Handsoldering -> MORNSUN:TD5(3)01MCANFD
- D14, D33, D4, D53, D6, D67: footprint Diode_SMD:D_SMA_Handsoldering -> Package_TO_SOT_SMD:SOT-23
- D15, D24, D27, D38, D39, D46, D52, D60, D66, D74: footprint LED_SMD:LED_0805_2012Metric -> Package_TO_SOT_SMD:SOT-23
- D16: footprint MORNSUN:K78xx-1000R3 -> Package_SO:SOIC-8_7.5x5.85mm_P1.27mm
- D17, D21, D25, D28, D43, D68, D71, D75, D77: footprint Package_TO_SOT_SMD:SOT-23 -> LED_SMD:LED_0805_2012Metric
- D18: footprint Package_TO_SOT_SMD:SOT-23 -> MORNSUN:WRB_S-3WR2
- D19: value ~ -> URB2405ZP-10WR3; footprint LED_SMD:LED_0805_2012Metric -> MORNSUN:URB_ZP-10WR3
- D2: footprint Package_TO_SOT_SMD:SOT-23 -> Package_SO:SOIC-8_7.5x5.85mm_P1.27mm
- D20: footprint LED_SMD:LED_0805_2012Metric -> Diode_SMD:D_SOD-123
- D22: value ~ -> BZX84C5V1; footprint LED_SMD:LED_0805_2012Metric -> Package_TO_SOT_SMD:SOT-23_Handsoldering
- D23, D29, D48, D51, D62, D65: footprint Package_TO_SOT_SMD:SOT-23 -> Diode_SMD:D_SMA_Handsoldering
- D26, D47, D50, D55, D57, D61, D64, D70, D8: footprint Diode_SMD:D_SMA_Handsoldering -> LED_SMD:LED_0805_2012Metric
- D3: footprint Diode_SMD:D_SOD-323_HandSoldering -> Package_TO_SOT_SMD:SOT-23
- D30, D42, D56, D58, D69, D72, D76: footprint LED_SMD:LED_0805_2012Metric -> Diode_SMD:D_SMA_Handsoldering
- D34, D35: footprint Package_SO:SOIC-8_7.5x5.85mm_P1.27mm -> LED_SMD:LED_0805_2012Metric
- D36: footprint Package_SO:SOIC-8_7.5x5.85mm_P1.27mm -> Diode_SMD:D_SMA_Handsoldering
- D37: footprint MORNSUN:WRB_S-3WR2 -> Diode_SMD:D_SMA_Handsoldering
- D41: footprint MORNSUN:K78xx-1000R3 -> LED_SMD:LED_0805_2012Metric
- D44: footprint Diode_SMD:D_SOD-123 -> Diode_SMD:D_SMA_Handsoldering
- D5: footprint Package_TO_SOT_SMD:SOT-23 -> Diode_SMD:D_SOD-323_HandSoldering
- D7: footprint Diode_SMD:D_SMA_Handsoldering -> Package_SO:SOIC-8_7.5x5.85mm_P1.27mm
- H3: value MountingHole_Pad -> MountingHole; footprint MountingHole:MountingHole_4.3mm_M4_Pad_Via -> MountingHole:MountingHole_4.3mm_M4
- H4: value MountingHole -> MountingHole_Pad; footprint MountingHole:MountingHole_4.3mm_M4 -> MountingHole:MountingHole_4.3mm_M4_Pad_Via
- J1: footprint Connector_Molex:Molex_Mini-Fit_Jr_5566-04A_2x02_P4.20mm_Vertical -> Connector_PinHeader_2.54mm:PinHeader_1x04_P2.54mm_Vertical
- J12, J21: footprint Connector_My:Mini-Fit_01x02_Vertical -> Connector_Molex:Molex_Mini-Fit_Jr_5566-04A_2x02_P4.20mm_Vertical
- J13: footprint Connector_Molex:Molex_Mini-Fit_Jr_5566-04A_2x02_P4.20mm_Vertical -> Connector_My:Mini-Fit_01x02_Vertical
- J3: footprint Connector_PinHeader_2.54mm:PinHeader_1x04_P2.54mm_Vertical -> Connector_My:Mini-Fit_01x02_Vertical
- Q1: footprint Package_TO_SOT_SMD:SOT-223 -> Package_TO_SOT_SMD:TO-252-2
- Q11: footprint Package_TO_SOT_SMD:TO-252-2 -> Package_TO_SOT_SMD:SOT-23
- Q12, Q14: footprint Package_TO_SOT_SMD:SOT-23 -> Package_TO_SOT_SMD:SOT-223
- Q17, Q3, Q5: footprint Package_TO_SOT_SMD:SOT-223 -> Package_TO_SOT_SMD:SOT-23
- R1, R42: value 10k -> 2M; footprint Resistor_SMD:R_0805_2012Metric_Pad1.20x1.40mm_HandSolder -> Resistor_SMD:R_1206_3216Metric
- R10: value 8.2k -> 49.9
- R100, R98: value 330 -> 10k
- R101, R109, R118, R60, R63, R70, R77, R83, R99: value 10k -> 8.2k
- R102, R108, R111, R117, R120, R128, R69, R80, R82, R92: value 8.2k -> 10k
- R103, R112, R121: value 10k -> 330
- R104, R107: value 330 -> 8.2k
- R105, R114, R58: value 8.2k -> 3.3k
- R106, R115, R97: value 10k -> 1k
- R11, R13, R4, R62, R72, R79: value 8.2k -> 1k
- R110, R119, R59, R61, R64: value 1k -> 10k
- R113, R116, R81, R91: value 1k -> 8.2k
- R12: value 10k -> 14k
- R122, R127: value 3.3k -> 8.2k
- R123, R67: value 10k -> 3.3k
- R124: value 3.3k -> 1k
- R14: value 1k -> 665
- R15, R46: value 2M -> 120; footprint Resistor_SMD:R_1206_3216Metric -> Resistor_SMD:R_0805_2012Metric_Pad1.20x1.40mm_HandSolder
- R16, R50, R88: value 2M -> 1k; footprint Resistor_SMD:R_1206_3216Metric -> Resistor_SMD:R_0805_2012Metric_Pad1.20x1.40mm_HandSolder
- R17, R8: value 120 -> 1k
- R18: value 16k -> 49.9; footprint Resistor_SMD:R_1206_3216Metric -> Resistor_SMD:R_0805_2012Metric_Pad1.20x1.40mm_HandSolder
- R19, R29: value 1k -> 120
- R2, R28, R3: value 1k -> 2M; footprint Resistor_SMD:R_0805_2012Metric_Pad1.20x1.40mm_HandSolder -> Resistor_SMD:R_1206_3216Metric
- R22: value 49.9 -> 1k
- R25, R6: value 120 -> 2M; footprint Resistor_SMD:R_0805_2012Metric_Pad1.20x1.40mm_HandSolder -> Resistor_SMD:R_1206_3216Metric
- R31, R48, R9: value 1k -> 16k; footprint Resistor_SMD:R_0805_2012Metric_Pad1.20x1.40mm_HandSolder -> Resistor_SMD:R_1206_3216Metric
- R32: value 665 -> 49.9
- R37: value 750 -> 8.2k
- R38: value 1.1k -> 750
- R39: value 49.9 -> 59
- R40: value 3.3k -> 2M; footprint Resistor_SMD:R_0805_2012Metric_Pad1.20x1.40mm_HandSolder -> Resistor_SMD:R_1206_3216Metric
- R41: value 8.2k -> 2M; footprint Resistor_SMD:R_0805_2012Metric_Pad1.20x1.40mm_HandSolder -> Resistor_SMD:R_1206_3216Metric
- R43: value 330 -> 1k
- R44: value 2M -> 16k
- R49: value 2M -> 49.9; footprint Resistor_SMD:R_1206_3216Metric -> Resistor_SMD:R_0805_2012Metric_Pad1.20x1.40mm_HandSolder
- R5: value 8.2k -> 16k; footprint Resistor_SMD:R_0805_2012Metric_Pad1.20x1.40mm_HandSolder -> Resistor_SMD:R_1206_3216Metric
- R51: value 2M -> 750; footprint Resistor_SMD:R_1206_3216Metric -> Resistor_SMD:R_0805_2012Metric_Pad1.20x1.40mm_HandSolder
- R52: value 16k -> 1k; footprint Resistor_SMD:R_1206_3216Metric -> Resistor_SMD:R_0805_2012Metric_Pad1.20x1.40mm_HandSolder
- R53: value 100 -> 100k
- R54: value 100k -> 2.4k; footprint Resistor_SMD:R_0805_2012Metric_Pad1.20x1.40mm_HandSolder -> Resistor_SMD:R_1206_3216Metric_Pad1.30x1.75mm_HandSolder
- R55: value 16k -> 1.1k; footprint Resistor_SMD:R_1206_3216Metric -> Resistor_SMD:R_0805_2012Metric_Pad1.20x1.40mm_HandSolder
- R56: value 49.9 -> 330
- R57: value 16k -> 8.2k; footprint Resistor_SMD:R_1206_3216Metric -> Resistor_SMD:R_0805_2012Metric_Pad1.20x1.40mm_HandSolder
- R65: value 3.3k -> 330
- R68: value 3.3k -> 232
- R7: value 14k -> 120
- R71: value 3.3k -> 10k
- R74: value 10k -> 100
- R75: value 750 -> 10k
- R84: value 49.9 -> 10k
- R85: value 120 -> 330
- R86: value 120 -> 8.2k
- R87: value 16k -> 3.3k; footprint Resistor_SMD:R_1206_3216Metric -> Resistor_SMD:R_0805_2012Metric_Pad1.20x1.40mm_HandSolder
- R89: value 2M -> 10k; footprint Resistor_SMD:R_1206_3216Metric -> Resistor_SMD:R_0805_2012Metric_Pad1.20x1.40mm_HandSolder
- R90: value 232 -> 8.2k
- R95: value 2.4k -> 8.2k; footprint Resistor_SMD:R_1206_3216Metric_Pad1.30x1.75mm_HandSolder -> Resistor_SMD:R_0805_2012Metric_Pad1.20x1.40mm_HandSolder
- R96: value 330 -> 3.3k
- U13, U16, U19, U25, U28: value PC817 -> RSCD06D3; footprint Package_DIP:DIP-4_W7.62mm -> OptoDevice:Finder_34.81
- U2: footprint Package_QFP:LQFP-100_14x14mm_P0.5mm -> Package_TO_SOT_SMD:SOT-23-5
- U20, U21, U23, U7, U9: value RSCD06D3 -> PC817; footprint OptoDevice:Finder_34.81 -> Package_DIP:DIP-4_W7.62mm
- U5: footprint Package_TO_SOT_SMD:SOT-23-5 -> Package_QFP:LQFP-100_14x14mm_P0.5mm
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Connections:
- C1 pad 1: +3.3V -> GND
- C1 pad 2: GND -> Net-(U1-+)
- C10 pad 1: +3.3V -> VDC_IN_SENSE
- C11 pad 1: +3.3V -> Net-(U3-+)
- C12 pad 1: +3.3V -> Net-(U1--)
- C12 pad 2: GND -> Net-(C12-Pad2)
- C13 pad 1: Net-(U2-PH1) -> +5V
- C14 pad 1: Net-(U2-VCAP_1) -> Crrent_Out
- C15 pad 1: Net-(U2-VCAP_2) -> Net-(U2-+)
- C16 pad 1: GND -> +3.3V
- C16 pad 2: CAN1_TXD_MCU -> GND
- C17 pad 1: GND -> +3.3V
- C17 pad 2: CANH -> GND
- C18 pad 1: GND -> +3.3V
- C18 pad 2: +3.3V -> GND
- C19 pad 1: GND -> +3.3V
- C19 pad 2: +3.3V -> GND
- C20 pad 1: CANL -> Current_SENSE
- C21 pad 1: +3.3V -> +24V_SENSE
- C22 pad 1: +3.3V -> GNDPWR
- C22 pad 2: GND -> +3.3VP
- C23 pad 1: VDC_IN_SENSE -> +3.3VP
- C23 pad 2: GND -> GNDPWR
- C24 pad 1: +3.3V -> GND
- C24 pad 2: GND -> +3.3V
- C25 pad 1: GND -> +3.3V
- C25 pad 2: +24V -> GND
- C26 pad 1: +3.3V -> GND
- C26 pad 2: GND -> Net-(U5-PH0)
- C27 pad 1: Net-(U4-+) -> +3.3V
- C28 pad 1: +24V_SENSE -> +3.3V
- C29 pad 1: Net-(U1--) -> +3.3V
- C29 pad 2: Net-(C29-Pad2) -> GND
- C30 pad 1: GND -> Net-(U5-PH1)
- C30 pad 2: Net-(U3-+) -> GND
- C32 pad 1: VDC_OUT1_SENSE -> +3.3V
- C33 pad 1: +24V -> +3.3V
- C34 pad 1: Net-(U3--) -> GND
- C34 pad 2: Net-(C34-Pad2) -> Net-(U4-+)
- C35 pad 1: GND -> +3.3V
- C35 pad 2: Net-(U5-+) -> GND
- C36 pad 1: +3.3V -> Net-(D7-VIN)
- C36 pad 2: GND -> GNDPWR
- C37 pad 1: VDC_OUT2_SENSE -> VDC_OUT1_SENSE
- C38 pad 1: Net-(U5--) -> Net-(U4--)
- C39 pad 1: Relay_1_ON -> GNDPWR
- C39 pad 2: GND -> +3.3VP
- C40 pad 1: Relay_2_ON -> +3.3VP
- C40 pad 2: GND -> GNDPWR
- C41 pad 1: Relay_3_ON -> GND
- C41 pad 2: GND -> +3.3V
- C42 pad 1: Relay_4_ON -> +3.3V
- C43 pad 1: Coil_5_CTRL -> +24V
- C44 pad 1: +3.3V -> GND
- C44 pad 2: GND -> +24V
- C45 pad 1: Current_SENSE -> +3.3V
- C46 pad 1: Net-(U6-+) -> +3.3V
- C47 pad 1: +3.3VP -> +3.3V
- C47 pad 2: GNDPWR -> GND
- C50 pad 1: GND -> +3.3V
- C50 pad 2: +3.3V -> GND
- C51 pad 1: +3.3V -> Net-(C51-Pad1)
- C51 pad 2: GND -> GND_CAN
- C52 pad 1: Net-(D35-VIN) -> Net-(U5-VCAP_1)
- C52 pad 2: GNDPWR -> GND
- C53 pad 1: GNDPWR -> Net-(U5-VCAP_2)
- C53 pad 2: +3.3VP -> GND
- C54 pad 1: +3.3VP -> GND
- C54 pad 2: GNDPWR -> Net-(U6-+)
- C55 pad 1: GND -> +3.3V
- C55 pad 2: +3.3V -> GND
- C56 pad 1: +3.3V -> Net-(D16-VIN)
- C56 pad 2: GND -> GNDPWR
- C57 pad 1: Net-(D36-VIN) -> Net-(D18-CS)
- C58 pad 1: GNDPWR -> +24V
- C58 pad 2: +3.3VP -> GND
- C59 pad 1: +3.3VP -> Net-(D18-Vin)
- C59 pad 2: GNDPWR -> GND
- C60 pad 1: GND -> VDC_OUT2_SENSE
- C60 pad 2: +3.3V -> GND
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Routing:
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- added copper zone on F.Cu, net Net-(U6--)
- removed copper zone on F.Cu, net +3.3V
- removed copper zone on F.Cu, net +5V
- removed copper zone on F.Cu, net Net-(D37-Vin)
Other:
- board text removed: "+24V"
- board text removed: "+5V"
- board text removed: "CANH"
- board text removed: "CANL"
- board text removed: "Current Sensor"
- board text removed: "Main Connector"
- board text removed: "OUT"
- board text removed: "PDU Control Board VER1.2"
- board text removed: "Precharge 1"
- board text removed: "Precharge 2"
- board text removed: "Shunt 1"
- board text removed: "Shunt 2"
- board text removed: "VDC_IN Enable"
